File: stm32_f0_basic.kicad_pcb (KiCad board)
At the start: 2 copper layers, 80 x 40 mm, 55 parts, among them J1 Conn_01x12_Male, J2 Conn_01x06_Male, J3 Conn_01x12_Male, J4 USB_B_Mini, J5 Conn_ARM_JTAG_SWD_10, SW1 B3S-1000P, SW2 B3S-1000P, U1 STM32F031K6Tx, U2 ADP121-AUJZ33R7, U3 FT230XS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

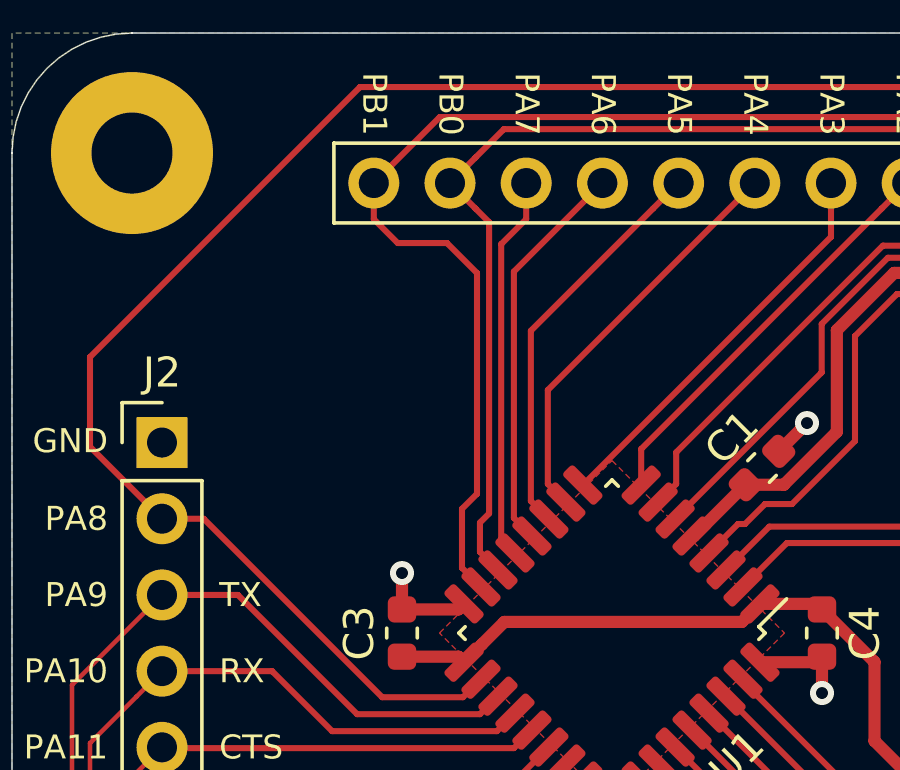
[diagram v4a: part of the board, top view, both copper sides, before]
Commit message: adjust traces and update TODO (3D models done)
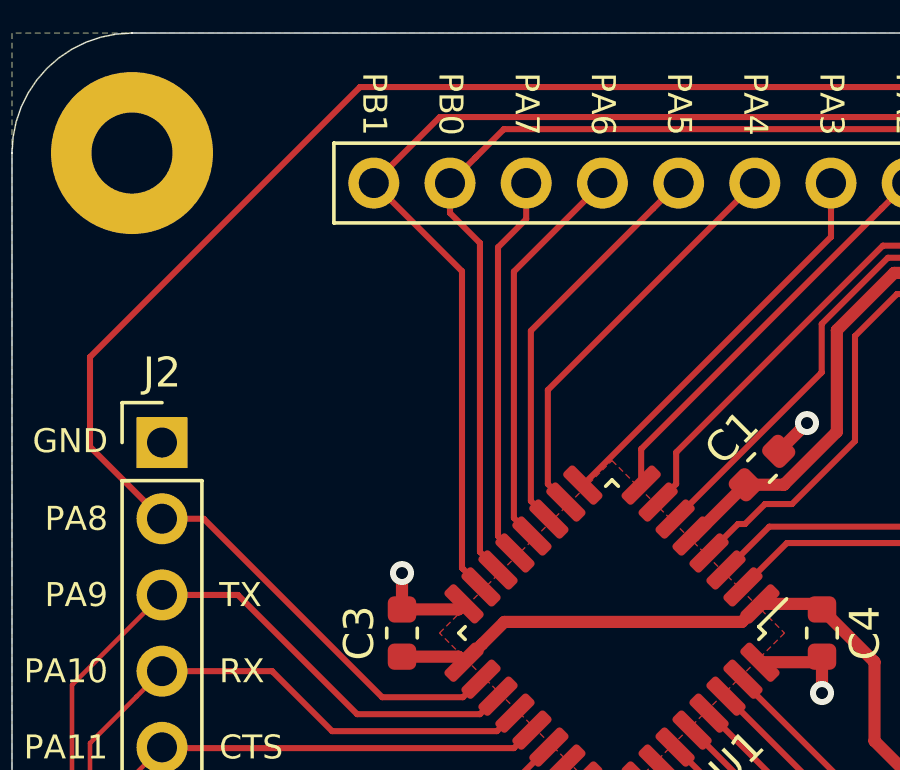
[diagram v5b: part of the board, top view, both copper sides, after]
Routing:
- net /stm32f0/PB1: track 52.2 -> 50.9 mm
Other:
- board text added: "TODO add OSHW/CC logos add project info to silk"
- board text removed: "TODO 3D models"
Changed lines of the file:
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@@
     (thickness 1.6)
     (drawings 13)
-    (tracks 514)
+    (tracks 508)
     (zones 0)
     (modules 55)
@@
   (gr_arc (start 196 91) (end 196 95) (angle -90) (layer Edge.Cuts) (width 0.05))
   (gr_arc (start 196 59) (end 200 59) (angle -90) (layer Edge.Cuts) (width 0.05))
-  (gr_text "TODO\n3D models" (at 201.5 57) (layer Cmts.User)
+  (gr_text "TODO\nadd OSHW/CC logos\nadd project info to silk" (at 201.5 57) (layer Cmts.User)
     (effects (font (size 1 1) (thickness 0.15)) (justify left))
   )
@@
   (segment (start 184 70.25) (end 179.5 70.25) (width 0.2032) (layer F.Cu) (net 10))
   (segment (start 177.125 92.5) (end 179.2125 92.5) (width 0.2032) (layer F.Cu) (net 11))
-  (segment (start 135.449999 60.849999) (end 134.6 60) (width 0.2032) (layer F.Cu) (net 12))
-  (segment (start 135.598262 72.295318) (end 135.598262 71.319351) (width 0.2032) (layer F.Cu) (net 12))
-  (segment (start 136.199301 72.896357) (end 135.598262 72.295318) (width 0.2032) (layer F.Cu) (net 12))
-  (segment (start 135.598262 71.319351) (end 135.90321 71.014403) (width 0.2032) (layer F.Cu) (net 12))
-  (segment (start 135.90321 71.014403) (end 135.90321 61.30321) (width 0.2032) (layer F.Cu) (net 12))
-  (segment (start 135.90321 61.30321) (end 135.449999 60.849999) (width 0.2032) (layer F.Cu) (net 12))
   (segment (start 136.396789 58.203211) (end 135.449999 59.150001) (width 0.2032) (layer F.Cu) (net 12))
   (segment (start 163.415711 58.203211) (end 136.396789 58.203211) (width 0.2032) (layer F.Cu) (net 12))
   (segment (start 164.6 59.3875) (end 163.415711 58.203211) (width 0.2032) (layer F.Cu) (net 12))
   (segment (start 135.449999 59.150001) (end 134.6 60) (width 0.2032) (layer F.Cu) (net 12))
+  (segment (start 134.6 61) (end 134.6 60) (width 0.2032) (layer F.Cu) (net 12))
+  (segment (start 136.199301 72.896357) (end 135.598262 72.295318) (width 0.2032) (layer F.Cu) (net 12))
+  (segment (start 135.598262 61.998262) (end 134.6 61) (width 0.2032) (layer F.Cu) (net 12))
+  (segment (start 135.598262 72.295318) (end 135.598262 61.998262) (width 0.2032) (layer F.Cu) (net 12))
   (segment (start 164.6 61.0125) (end 164.6 62.8125) (width 0.2032) (layer F.Cu) (net 13))
-  (segment (start 135 70.86) (end 135 72.828427) (width 0.2032) (layer F.Cu) (net 14))
-  (segment (start 135 72.828427) (end 135.633616 73.462043) (width 0.2032) (layer F.Cu) (net 14))
-  (segment (start 132.06 61.202081) (end 132.857919 62) (width 0.2032) (layer F.Cu) (net 14))
-  (segment (start 132.06 60) (end 132.06 61.202081) (width 0.2032) (layer F.Cu) (net 14))
-  (segment (start 132.857919 62) (end 134.5 62) (width 0.2032) (layer F.Cu) (net 14))
-  (segment (start 134.5 62) (end 135.5 63) (width 0.2032) (layer F.Cu) (net 14))
-  (segment (start 135.5 70.36) (end 135 70.86) (width 0.2032) (layer F.Cu) (net 14))
-  (segment (start 135.5 63) (end 135.5 70.36) (width 0.2032) (layer F.Cu) (net 14))
   (segment (start 132.06 60) (end 134.26 57.8) (width 0.2032) (layer F.Cu) (net 14))
   (segment (start 134.26 57.8) (end 164.8125 57.8) (width 0.2032) (layer F.Cu) (net 14))
   (segment (start 165.90572 58.89322) (end 166.4 59.3875) (width 0.2032) (layer F.Cu) (net 14))
   (segment (start 164.8125 57.8) (end 165.90572 58.89322) (width 0.2032) (layer F.Cu) (net 14))
+  (segment (start 135.032577 72.861004) (end 135.633616 73.462043) (width 0.2032) (layer F.Cu) (net 14))
+  (segment (start 135 72.828427) (end 135.032577 72.861004) (width 0.2032) (layer F.Cu) (net 14))
+  (segment (start 132.06 60) (end 135 62.94) (width 0.2032) (layer F.Cu) (net 14))
+  (segment (start 135 62.94) (end 135 72.828427) (width 0.2032) (layer F.Cu) (net 14))
   (segment (start 166.4 62.8125) (end 166.4 61.0125) (width 0.2032) (layer F.Cu) (net 15))
   (segment (start 188.5 91.5) (end 189 92) (width 0.4064) (layer F.Cu) (net 16))
@@
   (segment (start 184.7875 72.5) (end 186.4375 72.5) (width 0.2032) (layer F.Cu) (net 18))
   (segment (start 137.14 61.202081) (end 137.14 60) (width 0.2032) (layer F.Cu) (net 19))
-  (segment (start 136.764986 72.330672) (end 136.30642 71.872106) (width 0.2032) (layer F.Cu) (net 19))
-  (segment (start 136.30642 62.035661) (end 137.14 61.202081) (width 0.2032) (layer F.Cu) (net 19))
-  (segment (start 136.30642 71.872106) (end 136.30642 62.035661) (width 0.2032) (layer F.Cu) (net 19))
+  (segment (start 136.2 62.142081) (end 137.14 61.202081) (width 0.2032) (layer F.Cu) (net 19))
+  (segment (start 136.764986 72.330672) (end 136.2 71.765686) (width 0.2032) (layer F.Cu) (net 19))
+  (segment (start 136.2 71.765686) (end 136.2 62.142081) (width 0.2032) (layer F.Cu) (net 19))
   (segment (start 136.729633 71.163947) (end 137.330672 71.764986) (width 0.2032) (layer F.Cu) (net 20))
   (segment (start 136.729633 62.950367) (end 136.729633 71.163947) (width 0.2032) (layer F.Cu) (net 20))

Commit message: add Creative Commons/OSHW/Kicad/project info silkscreen
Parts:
- added LOGO1: Logo_Open_Hardware_Small, Symbol:OSHW-Symbol_6.7x6mm_SilkScreen, F.Cu at (167.4, 71.0)
- added LOGO2: CC-BY-SA_0.33in, Symbol_CreativeCommons:CC-BY-SA_SilkScreenTop_Small, F.Cu at (170.4, 80.2)
- added LOGO3: Logo_MadeWithKiCad, Symbol:KiCad-Logo2_5mm_SilkScreen, B.Cu at (145.6, 71.6)
- moved NT1 5.60 mm to (160.0, 71.6)
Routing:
- net VDD: track 130.1 -> 124.5 mm
- net VDDA: track 24.0 -> 28.7 mm
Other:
- board text added: "STM32F0 Basic Breakout Board G. Keeth 2019-10-20 https://github.com/gkeeth/stm32_f0_basic"
- board text added: "TODO adjust vias on bottom header (fix ground plane peninsula) add alternate pin function cheatsheet"
- board text removed: "TODO add OSHW/CC logos add project info to silk"

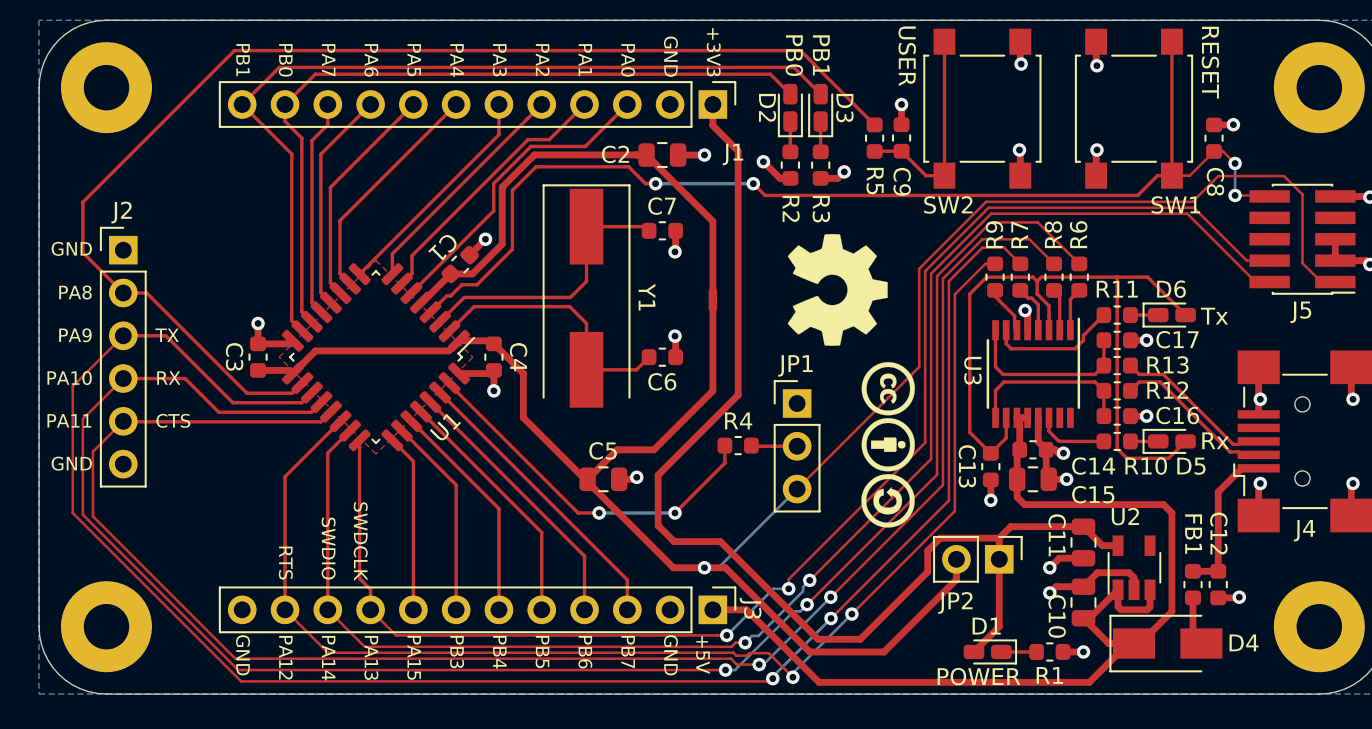
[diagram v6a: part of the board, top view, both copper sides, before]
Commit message: adjust ground plane, add pin silk reference
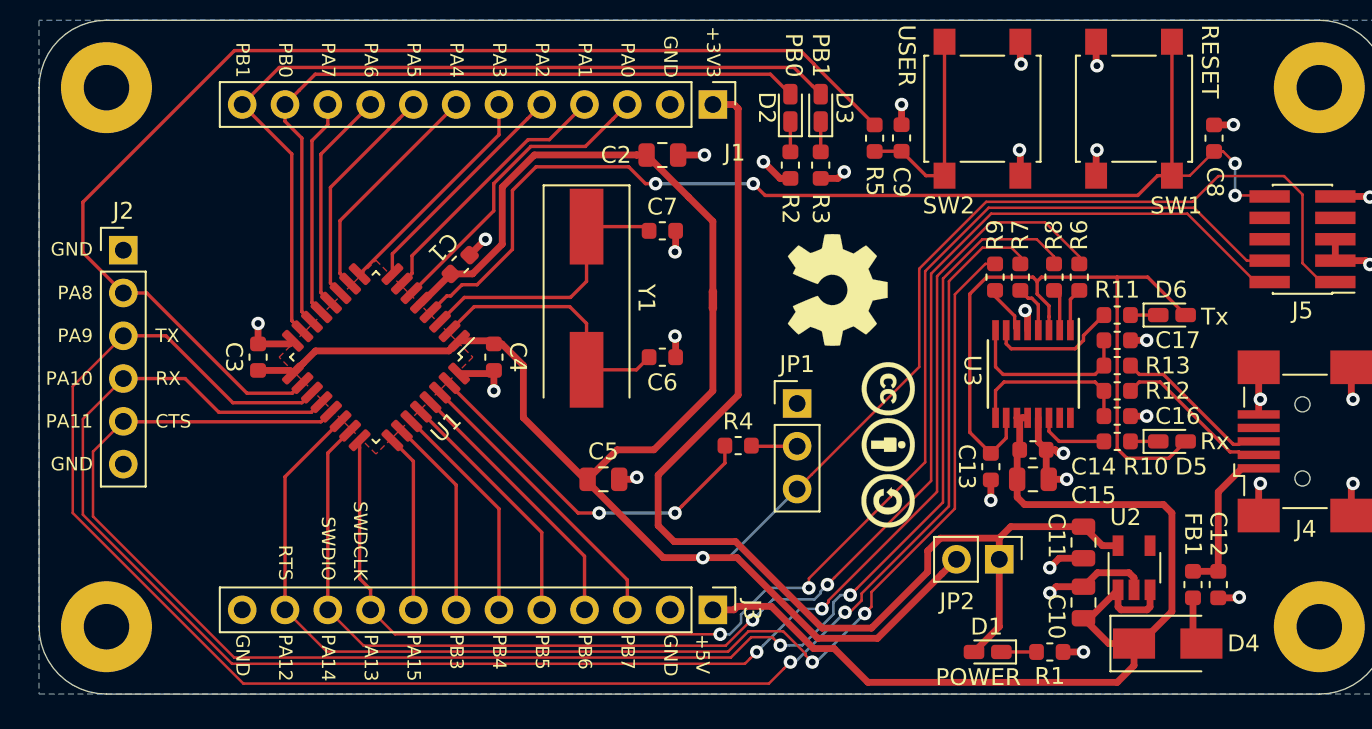
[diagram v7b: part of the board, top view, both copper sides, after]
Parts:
- moved LOGO3 15.7 mm to (136.0, 84.0)
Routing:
- net /stm32f0/PA11_USART1_CTS: track 97.9 -> 99.2 mm
- net VDD: track 124.5 -> 123.3 mm
- net +5V: track 62.1 -> 63.1 mm
- net /stm32f0/PA14_SWDCLK: track 82.5 -> 83.4 mm
- net /stm32f0/PA9_USART1_TX: track 104.0 -> 104.7 mm
- net /stm32f0/PA13_SWDIO: track 86.9 -> 87.5 mm
- net /stm32f0/PA10_USART1_RX: track 103.8 -> 104.4 mm
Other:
- board text added: "PA0 ADC_IN0 PA1 ADC_IN1 PA2 ADC_IN2 PA3 ADC_IN3 PA4 ADC_IN4 PA5 ADC_IN5 PA6 ADC_IN6 PA7 ADC_IN7"
- board text added: "PA8 BUTTON PA9 USART1_TX PA10 USART1_RX PA11 USART1_CTS PA12 USART1_RTS PA13 SWDIO PA14 SWCLK PA15 SPI1_NSS"
- board text added: "PB0 LED0 PB1 LED1 PB3 SPI1_SCK PB4 SPI1_MISO PB5 SPI1_MOSI PB6 I2C1_SCL PB7 I2C1_SDA"
- board text added: "STM32F0 Basic Breakout Board G. Keeth 2019-12-14 https://github.com/gkeeth/stm32_f0_basic"
- board text removed: "STM32F0 Basic Breakout Board G. Keeth 2019-10-20 https://github.com/gkeeth/stm32_f0_basic"
- board text removed: "TODO adjust vias on bottom header (fix ground plane peninsula) add alternate pin function cheatsheet"
